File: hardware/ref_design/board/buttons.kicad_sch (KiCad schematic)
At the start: 20 parts, among them SW1 P1 UP, SW10 P2 DOWN, SW11 P2 LEFT, SW12 P2 RIGHT, SW13 P2 A, SW14 P2 B, SW15 P2 X, SW16 P2 Y, SW2 P1 DOWN, SW20 P1 SELECT, SW21 P1 START / PWR, SW22 P2 SELECT, SW23 P2 START, SW3 P1 LEFT, SW4 P1 RIGHT, SW5 P1 A, SW6 P1 B, SW7 P1 X, SW8 P1 Y, SW9 P2 UP

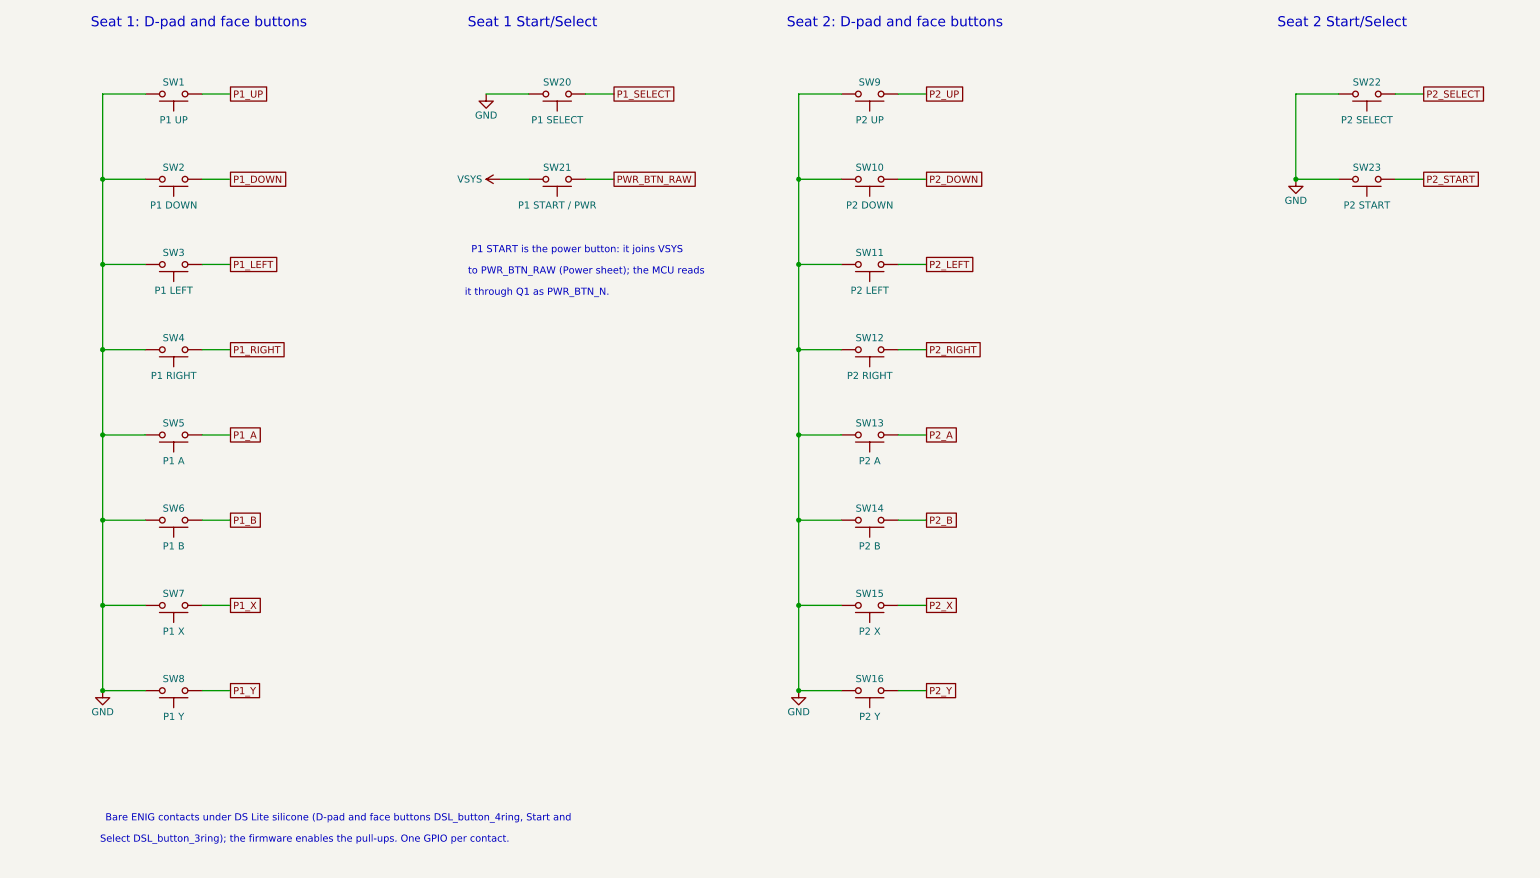
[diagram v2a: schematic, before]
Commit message: WIP: row 19 with shift registers and rows 1, 4, 16; 2 nets unrouted
The cell in a 54.0 x 37.0 mm hole, no speaker, every machine-placed part on
the top. New since the last WIP: each seat's D-pad and A/B/X/Y through a
74HC165 (SN74HC165PWR, chained, SR_PL/SR_CLK/SR_DATA on GPIO28-30, 10k
arrays); seat 2's Start powers on too (D8, R62, Q7, R63; P2_START on
GPIO34); Start/Select on 4 mm metal dome footprints; the BQ24073 power-path
charger in place of the TP4056 and its load sharing (pin reviews written);
the LDO beside the core; side screws at case (+-31.4, +-36); J1 at case
y -11. GPIO8 and GPIO11 (audio) unconnected.

Checks: check_netlist, check_pins and ERC pass (0). DRC: 0 errors, 8
cosmetic silkscreen warnings, 2 unconnected: QSPI_SS (U4 pin 75 to its
3.5 mm stub) and P1_SELECT (U4 pin 44 to SW20). check_fit: 17, all from
the case not knowing the moved screws, J1 and the dome vents yet.

Co-Authored-By: Claude Opus 5.5 <noreply@anthropic.com>
Claude-Session: https://claude.ai/code/session_01Y3mFMxLYqNeyyedvbYuRwX
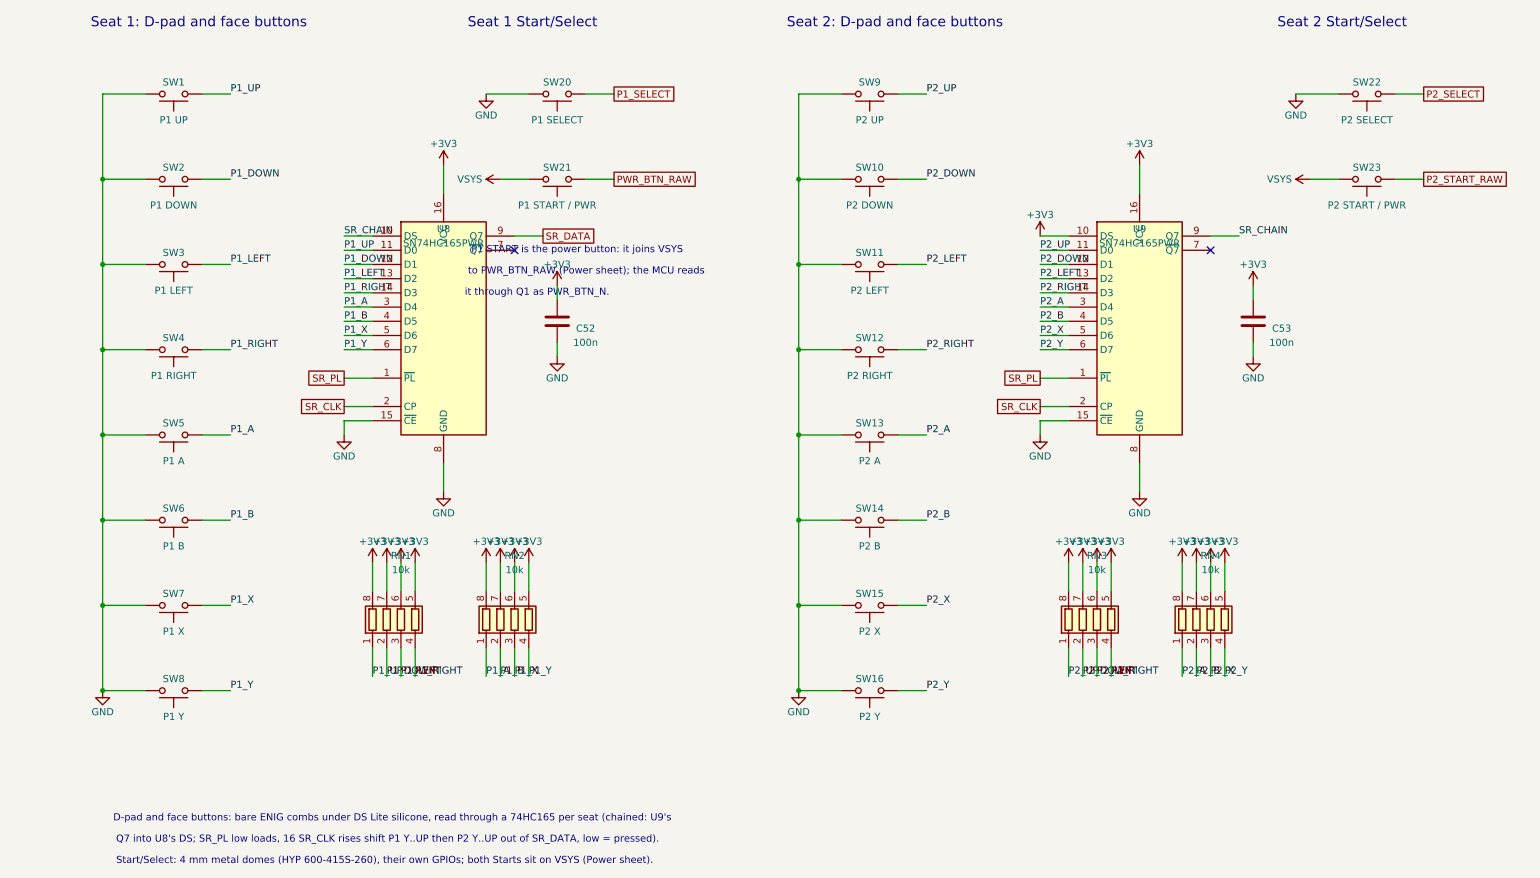
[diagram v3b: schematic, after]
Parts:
- added C52, C53: 100n, Capacitor_SMD:C_0402_1005Metric, symbol Device:C
- added RN1, RN2, RN3, RN4: 10k, Resistor_SMD:R_Array_Convex_4x0402, symbol Device:R_Pack04
- added U8, U9: SN74HC165PWR, Package_SO:TSSOP-16_4.4x5mm_P0.65mm, symbol 74xx:74HC165
- SW20, SW21, SW22: footprint battler:DSL_button_3ring -> battler:Dome_4mm_Round
- SW23: value P2 START -> P2 START / PWR; footprint battler:DSL_button_3ring -> battler:Dome_4mm_Round
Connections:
- net GND: now also C52.2, C53.2, U8.15 (~{CE}), U8.8 (GND), U9.15 (~{CE}), U9.8 (GND); no longer SW23.2
- net P1_A: now also RN2.1 (R1.1), U8.3 (D4)
- net P1_B: now also RN2.2 (R2.1), U8.4 (D5)
- net P1_DOWN: now also RN1.2 (R2.1), U8.12 (D1)
- net P1_LEFT: now also RN1.3 (R3.1), U8.13 (D2)
- net P1_RIGHT: now also RN1.4 (R4.1), U8.14 (D3)
- net P1_UP: now also RN1.1 (R1.1), U8.11 (D0)
- net P1_X: now also RN2.3 (R3.1), U8.5 (D6)
- net P1_Y: now also RN2.4 (R4.1), U8.6 (D7)
- net P2_A: now also RN4.1 (R1.1), U9.3 (D4)
- net P2_B: now also RN4.2 (R2.1), U9.4 (D5)
- net P2_DOWN: now also RN3.2 (R2.1), U9.12 (D1)
- net P2_LEFT: now also RN3.3 (R3.1), U9.13 (D2)
- net P2_RIGHT: now also RN3.4 (R4.1), U9.14 (D3)
- net P2_UP: now also RN3.1 (R1.1), U9.11 (D0)
- net P2_X: now also RN4.3 (R3.1), U9.5 (D6)
- net P2_Y: now also RN4.4 (R4.1), U9.6 (D7)
- net VSYS: now also SW23.2
- net P2_START renamed P2_START_RAW
- new net +3V3: C52.1, C53.1, RN1.5 (R4.2), RN1.6 (R3.2), RN1.7 (R2.2), RN1.8 (R1.2), RN2.5 (R4.2), RN2.6 (R3.2), RN2.7 (R2.2), RN2.8 (R1.2), RN3.5 (R4.2), RN3.6 (R3.2), RN3.7 (R2.2), RN3.8 (R1.2), RN4.5 (R4.2), RN4.6 (R3.2), RN4.7 (R2.2), RN4.8 (R1.2), U8.16 (VCC), U9.10 (DS), U9.16 (VCC)
- new net SR_CHAIN: U8.10 (DS), U9.9 (Q7)
- new net SR_CLK: U8.2 (CP), U9.2 (CP)
- new net SR_DATA: U8.9 (Q7)
- new net SR_PL: U8.1 (~{PL}), U9.1 (~{PL})
- no-connect marks 0 -> 2
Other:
- note added: "D-pad and face buttons: bare ENIG combs under DS Lite silicone, read through a 74HC165 per seat (chained: U9's"
- note added: "Q7 into U8's DS; SR_PL low loads, 16 SR_CLK rises shift P1 Y..UP then P2 Y..UP out of SR_DATA, low = pressed)."
- note added: "Start/Select: 4 mm metal domes (HYP 600-415S-260), their own GPIOs; both Starts sit on VSYS (Power sheet)."
- note removed: "Bare ENIG contacts under DS Lite silicone (D-pad and face buttons DSL_button_4ring, Start and"
- note removed: "Select DSL_button_3ring); the firmware enables the pull-ups. One GPIO per contact."

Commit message: ref_design: strips review: USB pair, SR_CLK series resistor, strip stitching, pinmap
Review of the strips beside the cell's hole (rows 1-4 of the review):
- USB D+/D-: route.py's usb_pair() draws them as one pair (0.2 mm, 0.3 apart) from
  J1 (D+ pads joined behind A7, D- at their tips) through U1, turned so each line
  runs over its own pin with no stub, then on the back to R21/R22. C1/R41 moved
  below the pair.
- SR_CLK: R65 (33 ohm, C25105, Basic) in series at the RP2354B's end, about 12 mm
  of track from pin 37, clear of the folded FPC. A 0.4 mm clock-to-SR_PL/SR_DATA
  clearance rule (and a GND guard track along each strip) left SR_CLK or SR_PL to
  U9 unrouted in five runs, so neither is in this board.
- Ground: strip_stitch() adds GND vias in the strips wherever both pours are filled.
- Flex: C47 turned with its long axis along the strip; the case asked for floor
  ribs under the strips (CELLCUT_FOR_CASE.md).
- docs/pinmap.md: both Starts as power buttons, SR_PL/SR_CLK/SR_DATA roles, the
  BQ24073 charger (no TP4056, CHG_DONE_N, D5/D7/Q2), 27 ohm USB resistors.

Routed clean (seed 7): DRC 0 errors, 0 unconnected; check_netlist, check_pins,
ERC pass; check_fit 17, the known case-side items.

Co-Authored-By: Claude Opus 5.5 <noreply@anthropic.com>
Claude-Session: https://claude.ai/code/session_01Y3mFMxLYqNeyyedvbYuRwX
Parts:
- added R65: 33, Resistor_SMD:R_0402_1005Metric, symbol Device:R
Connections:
- net SR_CLK: now also R65.2
- new net SR_CLK_MCU: R65.1
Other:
- note added: "SR_CLK source termination"
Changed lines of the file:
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@@
 	(wire
 		(pts
+			(xy 120.65 111.76) (xy 125.73 111.76)
+		)
+		(stroke
+			(width 0)
+			(type default)
+		)
+	)
+	(wire
+		(pts
+			(xy 133.35 111.76) (xy 138.43 111.76)
+		)
+		(stroke
+			(width 0)
+			(type default)
+		)
+	)
+	(wire
+		(pts
 			(xy 147.32 35.56) (xy 147.32 50.8)
 		)
@@
 		)
 	)
+	(text "SR_CLK source termination"
+		(exclude_from_sim no)
+		(at 135.1406 101.6 0)
+		(effects
+			(font
+				(size 1.8 1.8)
+			)
+		)
+	)
 	(text "D-pad and face buttons: bare ENIG combs under DS Lite silicone, read through a 74HC165 per seat (chained: U9's"
 		(exclude_from_sim no)
@@
 		)
 	)
-	(global_label "SR_CLK"
-		(shape passive)
-		(at 66.04 91.44 180)
-		(fields_autoplaced yes)
+	(label "SR_CLK"
+		(at 66.04 91.44 0)
 		(effects
 			(font
 				(size 1.27 1.27)
 			)
-			(justify right)
-		)
-		(property "Intersheetrefs" "${INTERSHEET_REFS}"
-			(at 66.04 91.44 0)
-			(hide yes)
-			(show_name no)
-			(do_not_autoplace no)
-			(effects
-				(font
-					(size 1.27 1.27)
-				)
-			)
+			(justify left bottom)
 		)
 	)
@@
 		)
 	)
-	(global_label "SR_CLK"
-		(shape passive)
-		(at 190.5 91.44 180)
-		(fields_autoplaced yes)
+	(label "SR_CLK"
+		(at 190.5 91.44 0)
 		(effects
 			(font
 				(size 1.27 1.27)
 			)
-			(justify right)
-		)
-		(property "Intersheetrefs" "${INTERSHEET_REFS}"
-			(at 190.5 91.44 0)
-			(hide yes)
-			(show_name no)
-			(do_not_autoplace no)
-			(effects
-				(font
-					(size 1.27 1.27)
-				)
-			)
+			(justify left bottom)
 		)
 	)
@@
 		)
 	)
+	(global_label "SR_CLK_MCU"
+		(shape passive)
+		(at 120.65 111.76 180)
+		(fields_autoplaced yes)
+		(effects
+			(font
+				(size 1.27 1.27)
+			)
+			(justify right)
+		)
+		(property "Intersheetrefs" "${INTERSHEET_REFS}"
+			(at 120.65 111.76 0)
+			(hide yes)
+			(show_name no)
+			(do_not_autoplace no)
+			(effects
+				(font
+					(size 1.27 1.27)
+				)
+			)
+		)
+	)
+	(label "SR_CLK"
+		(at 138.43 111.76 0)
+		(effects
+			(font
+				(size 1.27 1.27)
+			)
+			(justify left bottom)
+		)
+	)
 	(symbol
 		(lib_id "Switch:SW_Push")
@@
 					(unit 1)
 				)
+			)
+		)
+	)
+	(symbol
+		(lib_id "Device:R")
+		(at 129.54 111.76 90)
+		(unit 1)
+		(body_style 1)
+		(exclude_from_sim no)
+		(in_bom yes)
+		(on_board yes)
+		(in_pos_files yes)
+		(dnp no)
+		(property "Reference" "R65"
+			(at 129.54 109.144 90)
+			(show_name no)
+			(do_not_autoplace no)
+			(effects
+				(font
+					(size 1.27 1.27)
+				)
+			)
+		)
+		(property "Value" "33"
+			(at 129.54 114.376 90)
+			(show_name no)
+			(do_not_autoplace no)
+			(effects
+				(font
+					(size 1.27 1.27)
+				)
+			)
+		)
+		(property "Footprint" "Resistor_SMD:R_0402_1005Metric"
+			(at 129.54 111.76 0)
+			(hide yes)
+			(show_name no)
+			(do_not_autoplace no)
+			(effects
+				(font
+					(size 1.27 1.27)
+				)
+			)
+		)
+		(property "Datasheet" ""
+			(at 129.54 111.76 0)
+			(hide yes)
+			(show_name no)
+			(do_not_autoplace no)
+			(effects
+				(font
+					(size 1.27 1.27)
+				)
+			)
+		)
+		(property "Description" "Resistor"
+			(at 129.54 111.76 0)
+			(hide yes)
+			(show_name no)
+			(do_not_autoplace no)
+			(effects
+				(font
+					(size 1.27 1.27)
+				)
+			)
+		)
+		(property "LCSC" "C25105"
+			(at 129.54 111.76 0)
+			(hide yes)
+			(show_name no)
+			(do_not_autoplace no)
+			(effects
+				(font
+					(size 1.27 1.27)
+				)
+			)
+		)
+		(property "MPN" "0402WGF330JTCE"
+			(at 129.54 111.76 0)
+			(hide yes)
+			(show_name no)
+			(do_not_autoplace no)
+			(effects
+				(font
+					(size 1.27 1.27)
+				)
+			)
+		)
+		(property "Manufacturer" "UNI-ROYAL"
+			(at 129.54 111.76 0)
+			(hide yes)
+			(show_name no)
+			(do_not_autoplace no)
+			(effects
+				(font
+					(size 1.27 1.27)
+				)
+			)
+		)
+		(pin "1"
+		)
+		(pin "2"
+		)
+		(instances
+			(project "battler"
+				(path "/8922e0a8-6f76-52f6-b0ec-4de6a784796f/adaa66b2-a56d-591f-95e3-969ec1fb6ac3"
+					(reference "R65")
+					(unit 1)
+				)

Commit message: ref_design V&V round 3, schematic: R61 3.74k (DEC-31), R14 47k and R43 220k with no clamp (DEC-17), RN1-RN4 47k (DEC-24), U10 buffer on VBAT_SENSE, 10k B4460 NTC for TH1, J4 JST SH, pin reviews
Co-Authored-By: Claude Sonnet 5.5 <noreply@anthropic.com>
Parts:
- RN1, RN2, RN3, RN4: value 10k -> 47k; LCSC C25725 -> C2028; MPN 4D02WGJ0103TCE -> 4D02WGJ0473TCE
